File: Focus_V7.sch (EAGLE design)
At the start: 100 parts, among them X1 USB+SHIELD, Y1 16Mhz

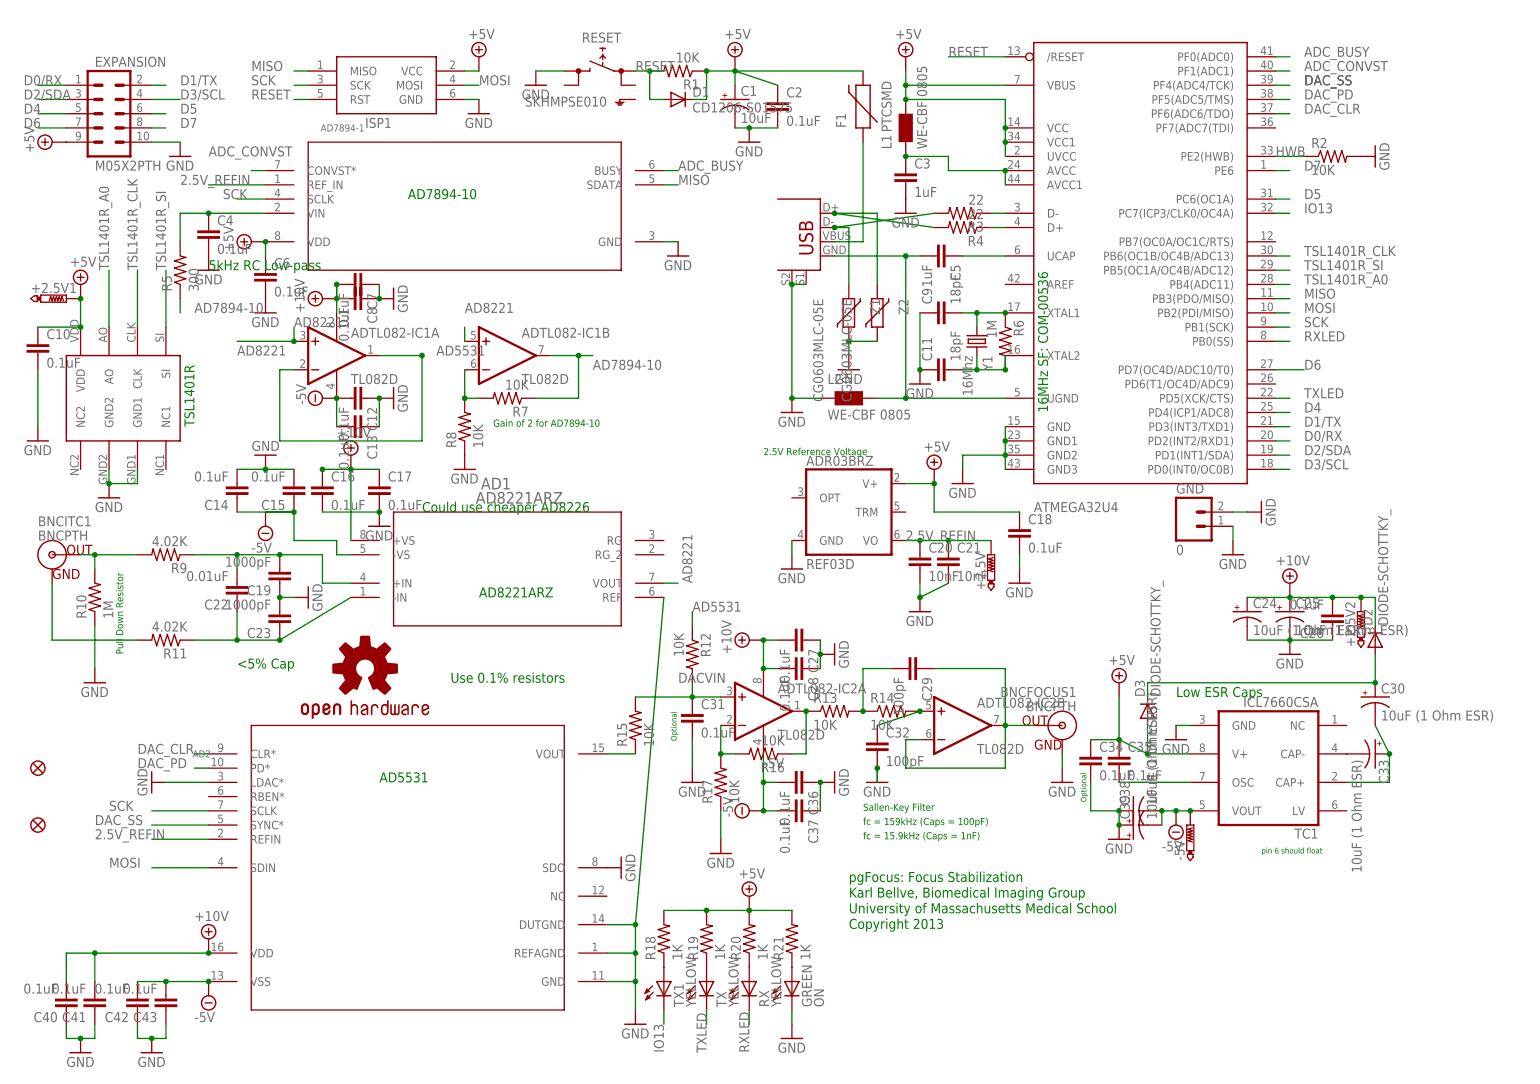
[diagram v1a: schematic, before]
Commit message: Pin 7 of TC7660 has a capacitor labeled C35, which should have been connected to ground, and not 5V This has been corrected in this revision. C35 is optional, and not needed. Only use if trying to slow down OSC for lower current.
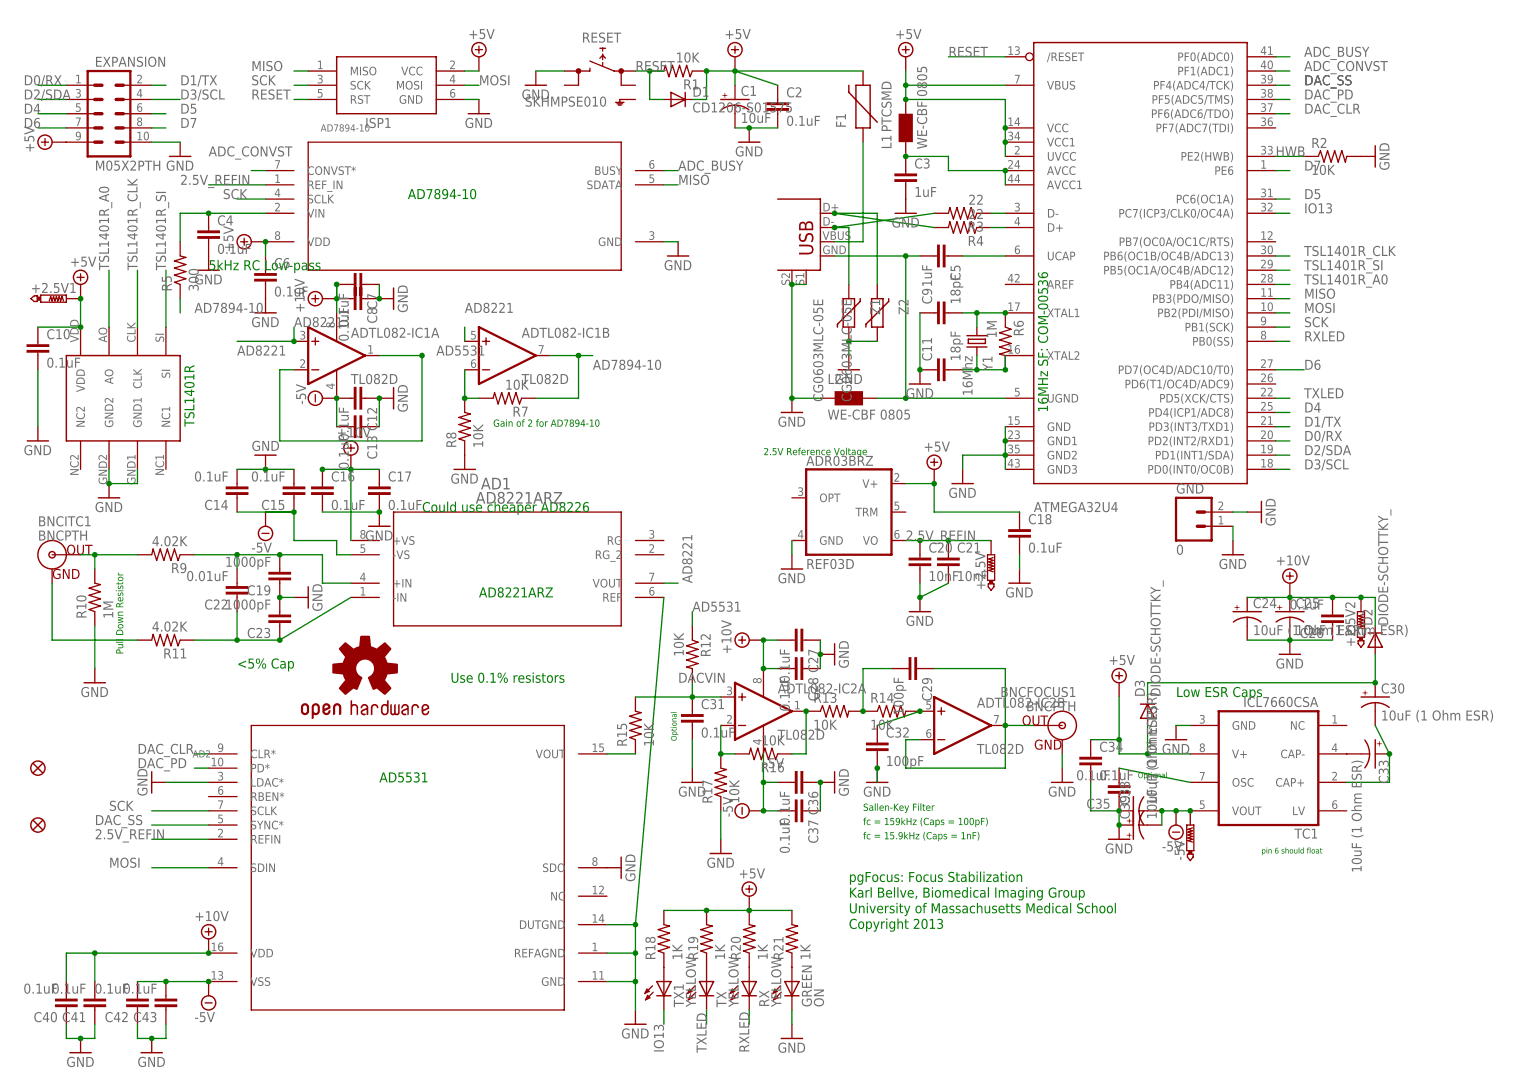
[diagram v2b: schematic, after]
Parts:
- renumbered AD7894-1 to AD7894-10
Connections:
- net +5V: no longer C35.1
- net GND: now also C35.1
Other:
- moved on the sheet: C35
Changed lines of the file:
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@@
 <part name="SUPPLY19" library="supply2" deviceset="+10V" device=""/>
 <part name="ADR03BRZ" library="linear" deviceset="REF03" device="D"/>
-<part name="AD7894-1" library="BIG" deviceset="AD7894ARZ-3" device=""/>
+<part name="AD7894-10" library="BIG" deviceset="AD7894ARZ-3" device=""/>
 <part name="SUPPLY15" library="supply2" deviceset="+5V" device=""/>
 <part name="C6" library="SparkFun" deviceset="CAP" device="0603-CAP" value="0.1uF"/>
@@
 <text x="15.24" y="104.14" size="1.778" layer="91">Could use cheaper AD8226</text>
 <text x="93.98" y="45.72" size="1.27" layer="91">fc = 15.9kHz (Caps = 1nF)</text>
-<text x="133.858" y="52.324" size="1.016" layer="91" rot="R90">Optional</text>
+<text x="148.336" y="57.658" size="1.016" layer="91" rot="R180">Optional</text>
 <text x="7.62" y="55.88" size="1.778" layer="91">AD5531</text>
 <text x="91.44" y="35.306" size="1.778" layer="91">Karl Bellve, Biomedical Imaging Group</text>
@@
 <instance part="SUPPLY19" gate="G$1" x="170.18" y="91.44"/>
 <instance part="ADR03BRZ" gate="A" x="91.44" y="104.14"/>
-<instance part="AD7894-1" gate="A" x="-12.7" y="165.1" smashed="yes">
+<instance part="AD7894-10" gate="A" x="-12.7" y="165.1" smashed="yes">
 <attribute name="NAME" x="-2.8702" y="172.085" size="1.27" layer="95" ratio="6" rot="SR0"/>
 </instance>
@@
 <instance part="L2" gate="G$1" x="91.44" y="121.92"/>
 <instance part="F1" gate="G$1" x="93.98" y="175.26" rot="R90"/>
-<instance part="C35" gate="G$1" x="139.7" y="58.42"/>
+<instance part="C35" gate="G$1" x="139.7" y="55.88" rot="R180"/>
 <instance part="C4" gate="G$1" x="-22.86" y="152.4"/>
 <instance part="GND3" gate="1" x="-22.86" y="147.32"/>
@@
 <pinref part="C34" gate="G$1" pin="2"/>
 <pinref part="C39" gate="G$1" pin="+"/>
+<pinref part="C35" gate="G$1" pin="1"/>
 </segment>
 <segment>
@@
 <segment>
 <wire x1="60.96" y1="152.4" x2="58.42" y2="152.4" width="0.1524" layer="91"/>
-<pinref part="AD7894-1" gate="A" pin="GND"/>
+<pinref part="AD7894-10" gate="A" pin="GND"/>
 <pinref part="GND31" gate="1" pin="GND"/>
 </segment>
@@
 <wire x1="-12.7" y1="160.02" x2="-17.78" y2="160.02" width="0.1524" layer="91"/>
 <label x="-20.32" y="160.02" size="1.778" layer="95"/>
-<pinref part="AD7894-1" gate="A" pin="SCLK"/>
+<pinref part="AD7894-10" gate="A" pin="SCLK"/>
 </segment>
 </net>
@@
 <wire x1="58.42" y1="162.56" x2="60.96" y2="162.56" width="0.1524" layer="91"/>
 <label x="60.96" y="162.56" size="1.778" layer="95"/>
-<pinref part="AD7894-1" gate="A" pin="SDATA"/>
+<pinref part="AD7894-10" gate="A" pin="SDATA"/>
 </segment>
 </net>
@@
 <net name="+5V" class="0">
 <segment>
-<wire x1="139.7" y1="63.5" x2="139.7" y2="71.12" width="0.1524" layer="91"/>
-<wire x1="152.4" y1="60.96" x2="144.78" y2="60.96" width="0.1524" layer="91"/>
-<wire x1="144.78" y1="66.04" x2="144.78" y2="60.96" width="0.1524" layer="91"/>
-<wire x1="144.78" y1="60.96" x2="139.7" y2="63.5" width="0.1524" layer="91"/>
-<wire x1="134.62" y1="63.5" x2="139.7" y2="63.5" width="0.1524" layer="91"/>
-<junction x="144.78" y="60.96"/>
-<junction x="139.7" y="63.5"/>
-<pinref part="SUPPLY11" gate="+5V" pin="+5V"/>
-<pinref part="TC1" gate="G$1" pin="V+"/>
-<pinref part="D3" gate="G$1" pin="A"/>
-<pinref part="C35" gate="G$1" pin="1"/>
-<pinref part="C34" gate="G$1" pin="1"/>
-</segment>
-<segment>
 <wire x1="-45.72" y1="137.16" x2="-45.72" y2="142.24" width="0.1524" layer="91"/>
 <wire x1="-53.34" y1="137.16" x2="-45.72" y2="137.16" width="0.1524" layer="91"/>
@@
 <wire x1="-12.7" y1="152.4" x2="-12.7" y2="149.86" width="0.1524" layer="91"/>
 <junction x="-12.7" y="152.4"/>
-<pinref part="AD7894-1" gate="A" pin="VDD"/>
+<pinref part="AD7894-10" gate="A" pin="VDD"/>
 <pinref part="SUPPLY15" gate="+5V" pin="+5V"/>
 <pinref part="C6" gate="G$1" pin="1"/>
@@
 <pinref part="R18" gate="G$1" pin="2"/>
 </segment>
+<segment>
+<wire x1="152.4" y1="60.96" x2="144.78" y2="60.96" width="0.1524" layer="91"/>
+<wire x1="144.78" y1="66.04" x2="144.78" y2="60.96" width="0.1524" layer="91"/>
+<pinref part="TC1" gate="G$1" pin="V+"/>
+<pinref part="D3" gate="G$1" pin="A"/>
+<pinref part="SUPPLY11" gate="+5V" pin="+5V"/>
+<wire x1="144.78" y1="60.96" x2="139.7" y2="60.96" width="0.1524" layer="91"/>
+<wire x1="139.7" y1="60.96" x2="139.7" y2="63.5" width="0.1524" layer="91"/>
+<junction x="144.78" y="60.96"/>
+<pinref part="C34" gate="G$1" pin="1"/>
+<wire x1="139.7" y1="63.5" x2="139.7" y2="71.12" width="0.1524" layer="91"/>
+<wire x1="134.62" y1="63.5" x2="139.7" y2="63.5" width="0.1524" layer="91"/>
+<junction x="139.7" y="63.5"/>
+</segment>
 </net>
 <net name="N$30" class="0">
@@
 <wire x1="-12.7" y1="162.56" x2="-22.86" y2="162.56" width="0.1524" layer="91"/>
 <label x="-27.94" y="162.56" size="1.778" layer="95"/>
-<pinref part="AD7894-1" gate="A" pin="REF_IN"/>
+<pinref part="AD7894-10" gate="A" pin="REF_IN"/>
 </segment>
 </net>
@@
 <wire x1="58.42" y1="165.1" x2="60.96" y2="165.1" width="0.1524" layer="91"/>
 <label x="60.96" y="165.1" size="1.778" layer="95"/>
-<pinref part="AD7894-1" gate="A" pin="BUSY"/>
+<pinref part="AD7894-10" gate="A" pin="BUSY"/>
 </segment>
 <segment>
@@
 <net name="N$5" class="0">
 <segment>
-<wire x1="152.4" y1="55.88" x2="139.7" y2="55.88" width="0.1524" layer="91"/>
+<wire x1="152.4" y1="55.88" x2="139.7" y2="58.42" width="0.1524" layer="91"/>
 <pinref part="TC1" gate="G$1" pin="OSC"/>
 <pinref part="C35" gate="G$1" pin="2"/>
@@
 <wire x1="-12.7" y1="165.1" x2="-15.24" y2="165.1" width="0.1524" layer="91"/>
 <label x="-22.86" y="167.64" size="1.778" layer="95"/>
-<pinref part="AD7894-1" gate="A" pin="CONVST*"/>
+<pinref part="AD7894-10" gate="A" pin="CONVST*"/>
 </segment>
 <segment>
@@
 <wire x1="-27.94" y1="157.48" x2="-27.94" y2="152.4" width="0.1524" layer="91"/>
 <junction x="-22.86" y="157.48"/>
-<pinref part="AD7894-1" gate="A" pin="VIN"/>
+<pinref part="AD7894-10" gate="A" pin="VIN"/>
 <pinref part="C4" gate="G$1" pin="1"/>
 <pinref part="R5" gate="G$1" pin="2"/>

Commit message: LDAC pin of AD5531 needs to be tied to ground, Clean up of text
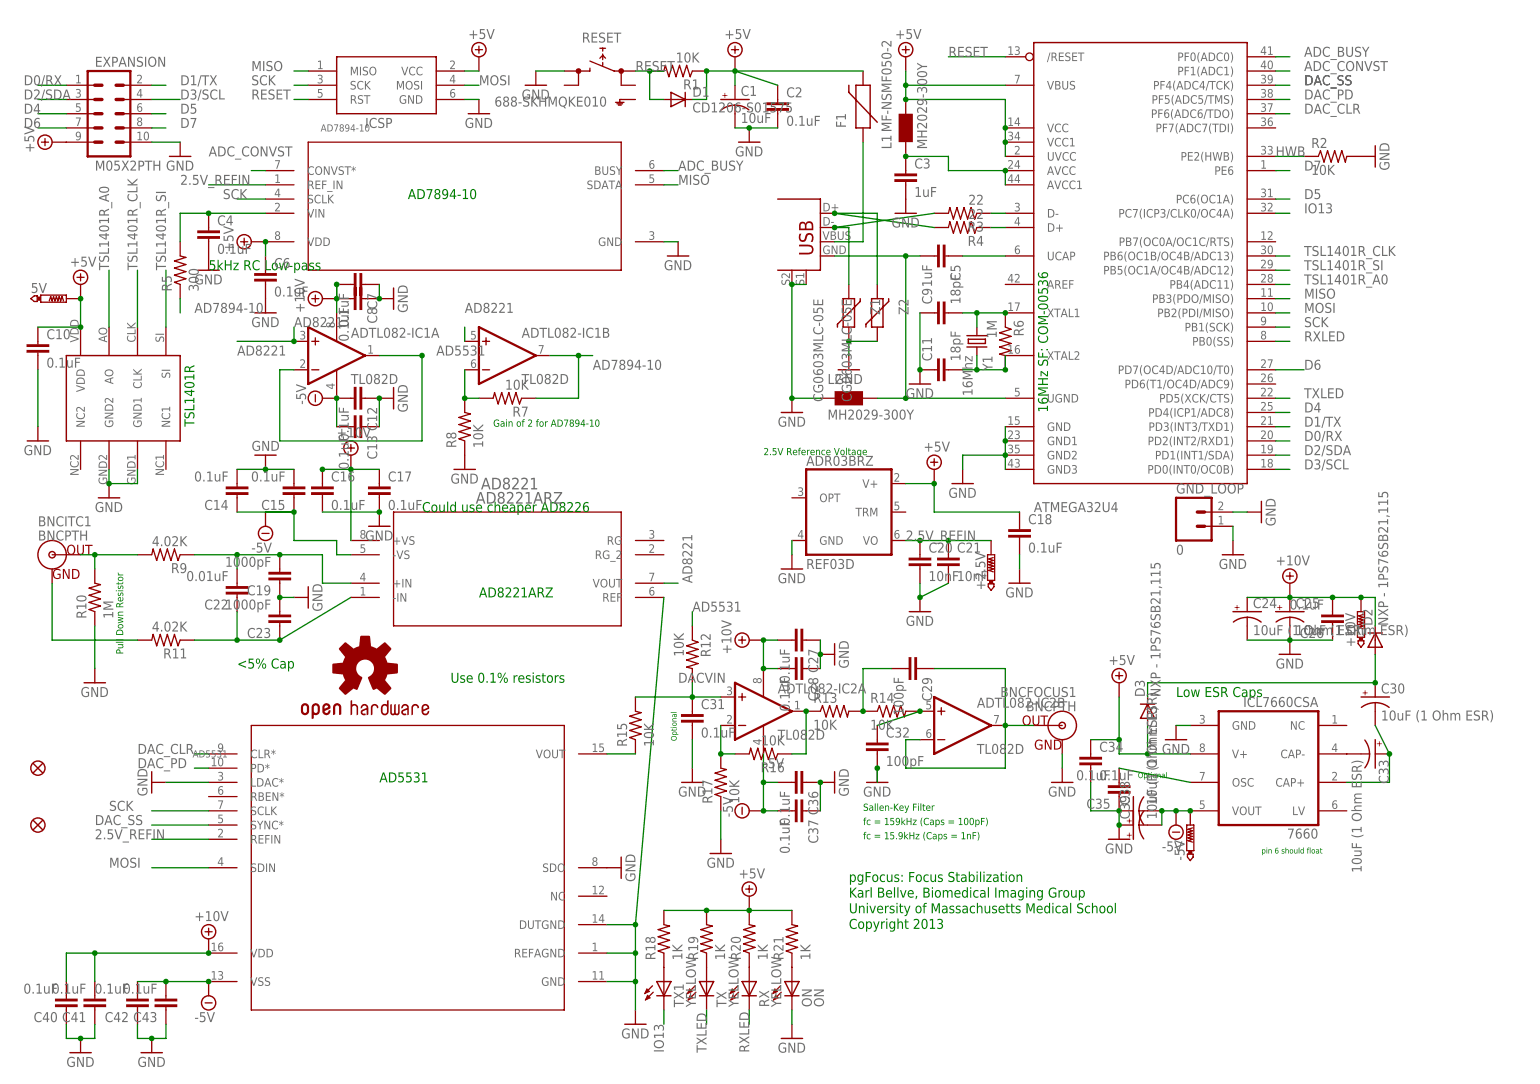
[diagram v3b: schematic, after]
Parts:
- AD7894-10: value AD7894ARZ-3 -> AD7894ARZ-10
- D2, D3: value DIODE-SCHOTTKY_ -> NXP - 1PS76SB21,115
- F1: value PTCSMD -> MF-NSMF050-2
- L1, L2: value WE-CBF 0805 -> MH2029-300Y
- RESET: value SKHMPSE010 -> 688-SKHMQKE010
- renumbered +2.5V1 to 5V, +2.5V2 to +10V, AD1 to AD8221, AD2 to AD5531, GND to GND_LOOP, GREEN to ON, ISP1 to ICSP, TC1 to 7660
